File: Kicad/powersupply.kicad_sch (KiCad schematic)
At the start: 26 parts, among them J1101 Jack 2.1{slash}6.3mm, J1102 2x2 Socket, J1103 4-pin Socket, Q1101 SS8050, Q1102 AO3401A, Q1103 SS8550, U1101 DC-DC Module, U1102 LP2950N, U1103 AMS1117-3.3

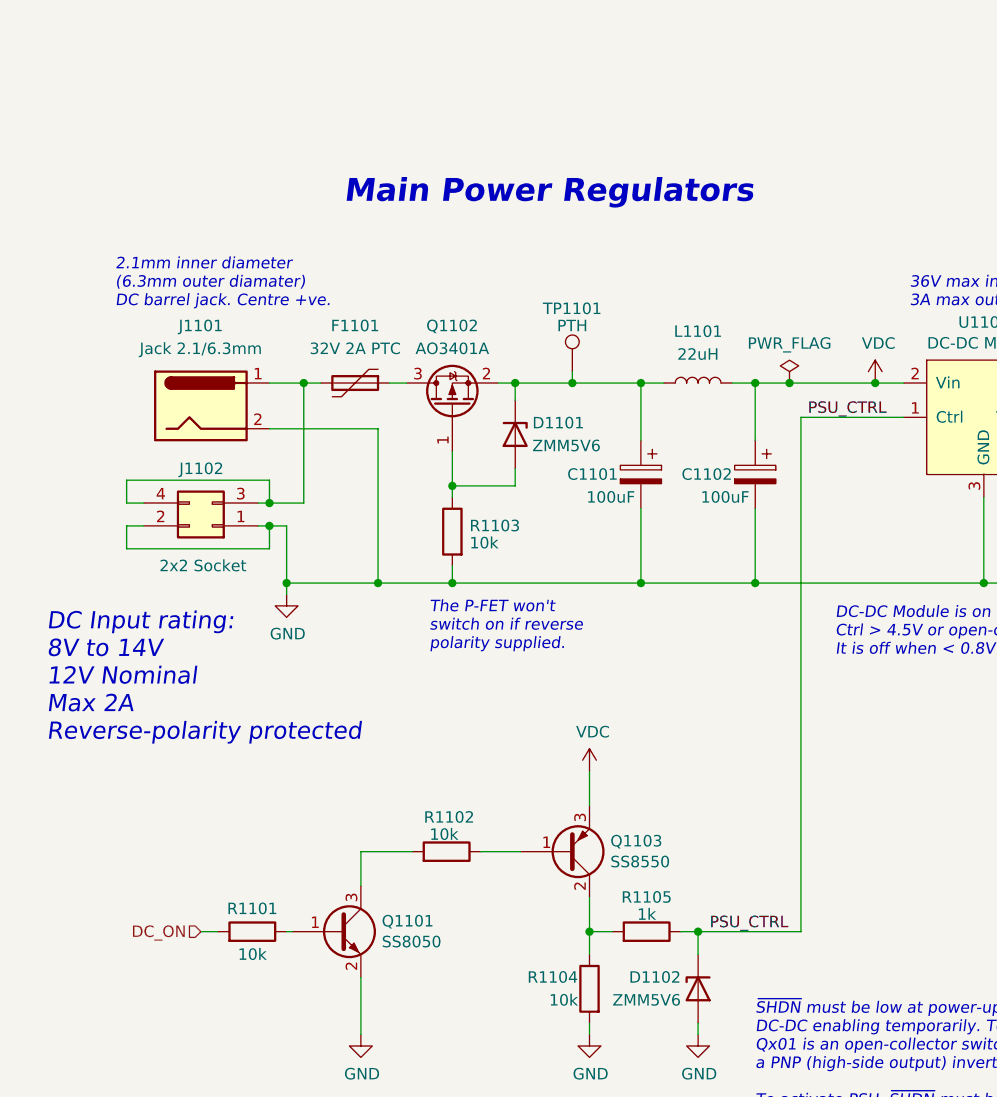
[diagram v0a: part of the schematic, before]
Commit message: Re-organised top sheet.
Lots of parts just changed their component designator. I had
to patch up the PCB manually, but now it imports from the schematic
OK.

Also adds two PSU rails for the RTC (so you can pick DS1307
which is a 5V part, or MCP7940N which is a 3.3V part).
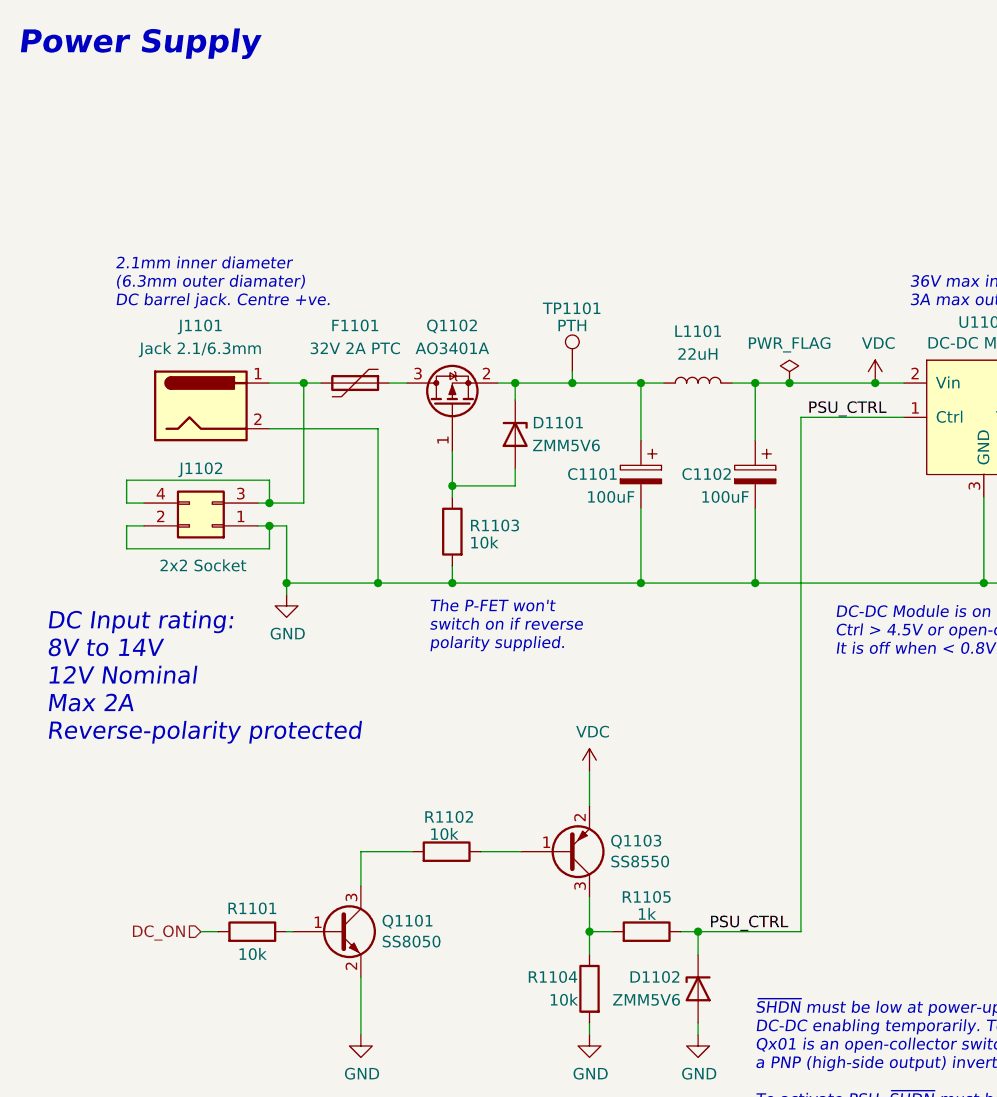
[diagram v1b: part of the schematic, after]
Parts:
- Q1101: symbol Transistor_BJT:S8050 -> Transistor_BJT:BC817; LCSC Part# C105432 -> C2150; MPN S8050 -> SS8050
- Q1103: symbol Transistor_BJT:BC556 -> Transistor_BJT:BC807
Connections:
- net VDC: now also Q1103.2 (E); no longer Q1103.3 (E)
- net at R1104.1, R1105.2: now also Q1103.3 (C); no longer Q1103.2 (C)
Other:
- note added: "Power Supply"
- note removed: "Main Power Regulators"
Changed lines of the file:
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@@
     (effects (font (size 1.27 1.27) italic) (justify left bottom))
   )
-  (text "Main Power Regulators" (at 48.895 34.29 0)
+  (text "Power Supply" (at 12.7 17.78 0)
     (effects (font (size 2.54 2.54) (thickness 0.508) bold italic) (justify left bottom))
   )
@@
     (pin "1")
   )
-  (symbol (lib_id "Transistor_BJT:S8050") (at 48.26 114.935 0) (unit 1)
+  (symbol (lib_id "Transistor_BJT:BC817") (at 48.26 114.935 0) (unit 1)
     (in_bom yes) (on_board yes)
     (property "Reference" "Q1101" (id 0) (at 53.1114 113.7666 0)
@@
       (effects (font (size 1.27 1.27) italic) (justify left) hide)
     )
-    (property "Datasheet" "http://www.unisonic.com.tw/datasheet/S8050.pdf" (id 3) (at 48.26 114.935 0)
+    (property "Datasheet" "https://datasheet.lcsc.com/lcsc/1811052004_Jiangsu-Changjing-Electronics-Technology-Co---Ltd--SS8050_C2150.pdf" (id 3) (at 48.26 114.935 0)
       (effects (font (size 1.27 1.27)) (justify left) hide)
     )
@@
       (effects (font (size 1.27 1.27)) hide)
     )
-    (property "MPN" "S8050" (id 5) (at 48.26 114.935 0)
+    (property "MPN" "SS8050" (id 5) (at 48.26 114.935 0)
       (effects (font (size 1.27 1.27)) hide)
     )
@@
       (effects (font (size 1.27 1.27)) hide)
     )
-    (property "LCSC Part#" "C105432" (id 8) (at 48.26 114.935 0)
+    (property "LCSC Part#" "C2150" (id 8) (at 48.26 114.935 0)
       (effects (font (size 1.27 1.27)) hide)
     )
@@
     (pin "1")
   )
-  (symbol (lib_id "Transistor_BJT:BC556") (at 73.66 106.045 0) (mirror x) (unit 1)
+  (symbol (lib_id "Transistor_BJT:BC807") (at 73.66 106.045 0) (mirror x) (unit 1)
     (in_bom yes) (on_board yes)
     (property "Reference" "Q1103" (id 0) (at 78.5114 104.8766 0)

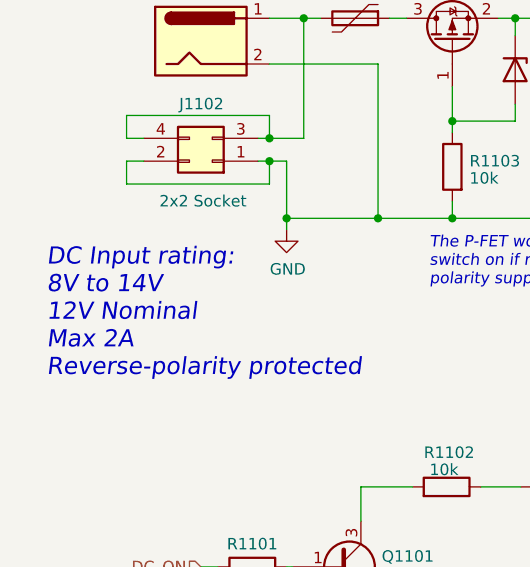
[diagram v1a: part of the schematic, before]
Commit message: Documentation updates.
Also moved a wire on the IO page, and amended some doc comments
in the schematic. Notably the Power Input limit is now 30V because
of the Zener on the control line.
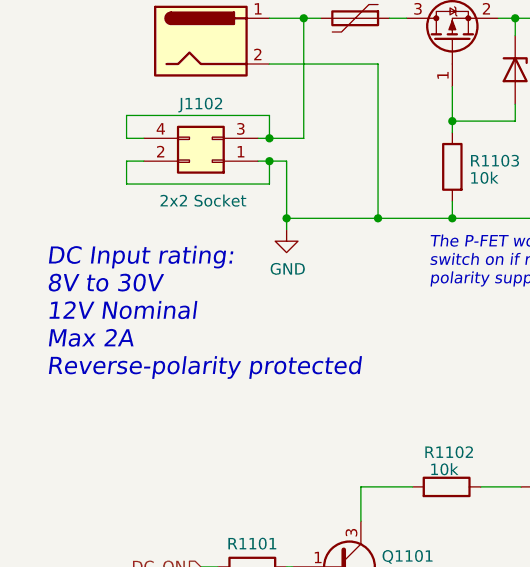
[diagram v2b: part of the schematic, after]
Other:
- note added: "DC Input rating: 8V to 30V 12V Nominal Max 2A Reverse-polarity protected"
- note removed: "DC Input rating: 8V to 14V 12V Nominal Max 2A Reverse-polarity protected"
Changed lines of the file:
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@@
     (effects (font (size 1.27 1.27) italic) (justify left bottom))
   )
-  (text "DC Input rating:\n8V to 14V\n12V Nominal\nMax 2A\nReverse-polarity protected"
+  (text "DC Input rating:\n8V to 30V\n12V Nominal\nMax 2A\nReverse-polarity protected"
     (at 15.875 93.98 0)
     (effects (font (size 1.905 1.905) italic) (justify left bottom))

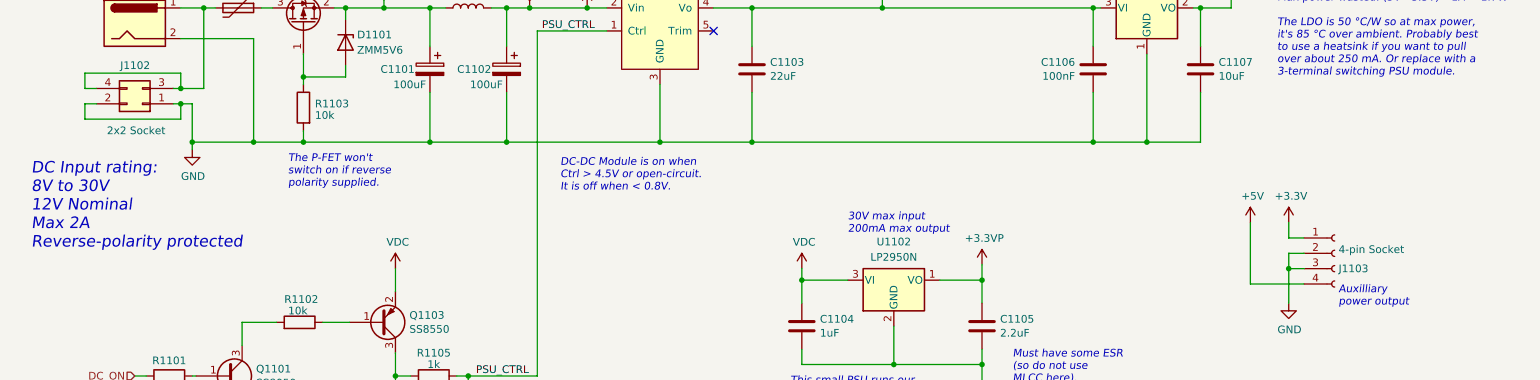
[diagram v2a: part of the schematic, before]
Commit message: Cleaned up the part numbers.
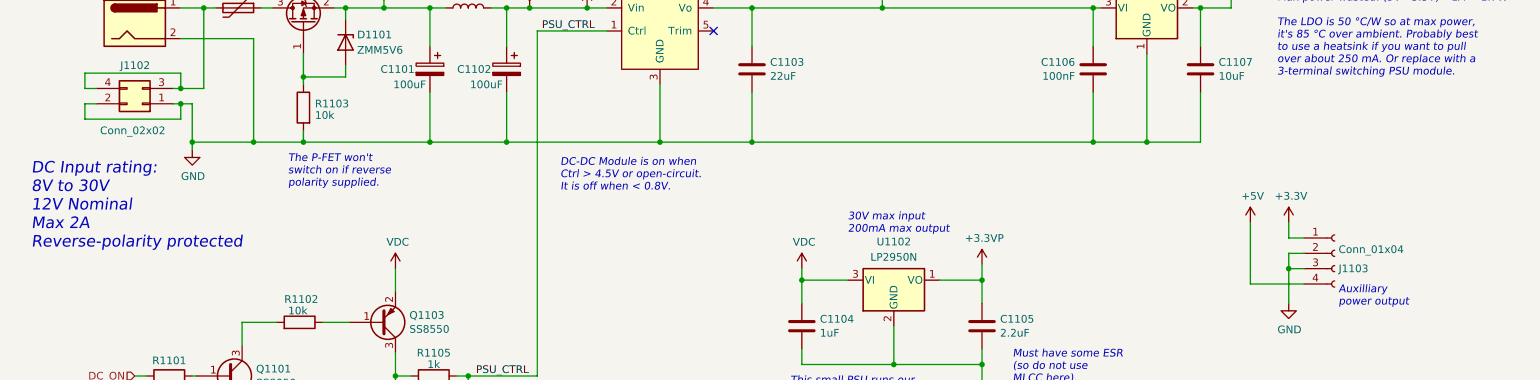
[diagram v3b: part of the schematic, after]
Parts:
- C1103: Digikey 490-3886-1-ND -> (none); JLCPCB Collection (none) -> Extended; Mouser 187-CL21A226MAYNNNE -> (none); Voltage 16V -> 25V
- C1104: Digikey 311-1456-1-ND -> (none); JLCPCB Collection (none) -> Basic; MPN CC0805KKX7R8BB105 -> CL21B105KBFNNNE; Manufacturer Yageo -> Samsung; Mouser 603-CC805KKX7R8BB105 -> (none); Tolerance X5R -> X7R; Voltage 25V -> 50V
- C1105: Digikey PCE4027CT-ND -> (none); JLCPCB Collection (none) -> Extended; MPN EEE-FC1V2R2R -> RVT1C2R2M0405; Manufacturer Panasonic -> Roqang; Mouser 667-EEE-FC1V2R2R -> (none); Voltage 10V -> 16V
- C1106: Digikey 399-C0805C104M5RAC7800CT-ND -> (none); JLCPCB Collection (none) -> Basic; MPN C0805C104M5RACTU -> CC0805KRX7R9BB104; Manufacturer Kemet -> Yageo; Mouser 80-C0805C104M5R -> (none); Tolerance X5R -> X7R; Voltage 16V -> 50V
- C1107: Digikey 490-3886-1-ND -> (none); JLCPCB Collection (none) -> Basic; MPN GRM21BR61C106KE15L -> CL21A106KAYNNNE; Manufacturer Murata -> Samsung; Mouser 81-GRM21BR61C106KE15 -> (none); Voltage 16V -> 25V
- D1101, D1102: Digikey 1727-1888-2-ND -> (none); JLCPCB Collection (none) -> Basic; MPN ZMM5V6 -> ZMM5V6-M
- J1102: value 2x2 Socket -> Conn_02x02
- J1103: value 4-pin Socket -> Conn_01x04
- Q1101: Digikey MMSS8050-L-TPMSCT-ND -> (none); JLCPCB Collection (none) -> Basic; Manufacturer JCET -> JSCJ; Voltage (none) -> 25V
- Q1102: Digikey 785-1001-2-ND -> (none); JLCPCB Collection (none) -> Basic
- Q1103: Digikey MMSS8550-L-TPMSCT-ND -> (none); JLCPCB Collection (none) -> Basic; MPN SS8550 -> SS8550 Y2; Manufacturer JCET -> JSCJ; Voltage (none) -> 25V
- R1101, R1102, R1103, R1104: Digikey RMCF0805FT10K0CT-ND -> (none); JLCPCB Collection (none) -> Basic; MPN RMCF0805FT10K0 -> 0805W8F1002T5E; Manufacturer Stackpole -> Uniroyal
- R1105: Digikey RMCF0805FT1K00CT-ND -> (none); JLCPCB Collection (none) -> Basic; MPN RMCF0805FT1K00 -> 0805W8F1001T5E; Manufacturer Stackpole -> Uniroyal
- U1103: Digikey NCP1117ST33T3GOSCT-ND -> (none); JLCPCB Collection (none) -> Basic; MPN NCP1117ST33T3GOS -> AMS1117-3.3; Manufacturer ON Semiconductor -> AMS; Mouser 863-NCP1117ST33T3G -> (none)
